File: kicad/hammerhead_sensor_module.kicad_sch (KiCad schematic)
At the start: 27 parts, among them J1 COMMS CONN, J10 12402012E212A, J9 B6B-XH-A, U16 TPD4E05U06DQAR, U4 TPD4E05U06DQAR

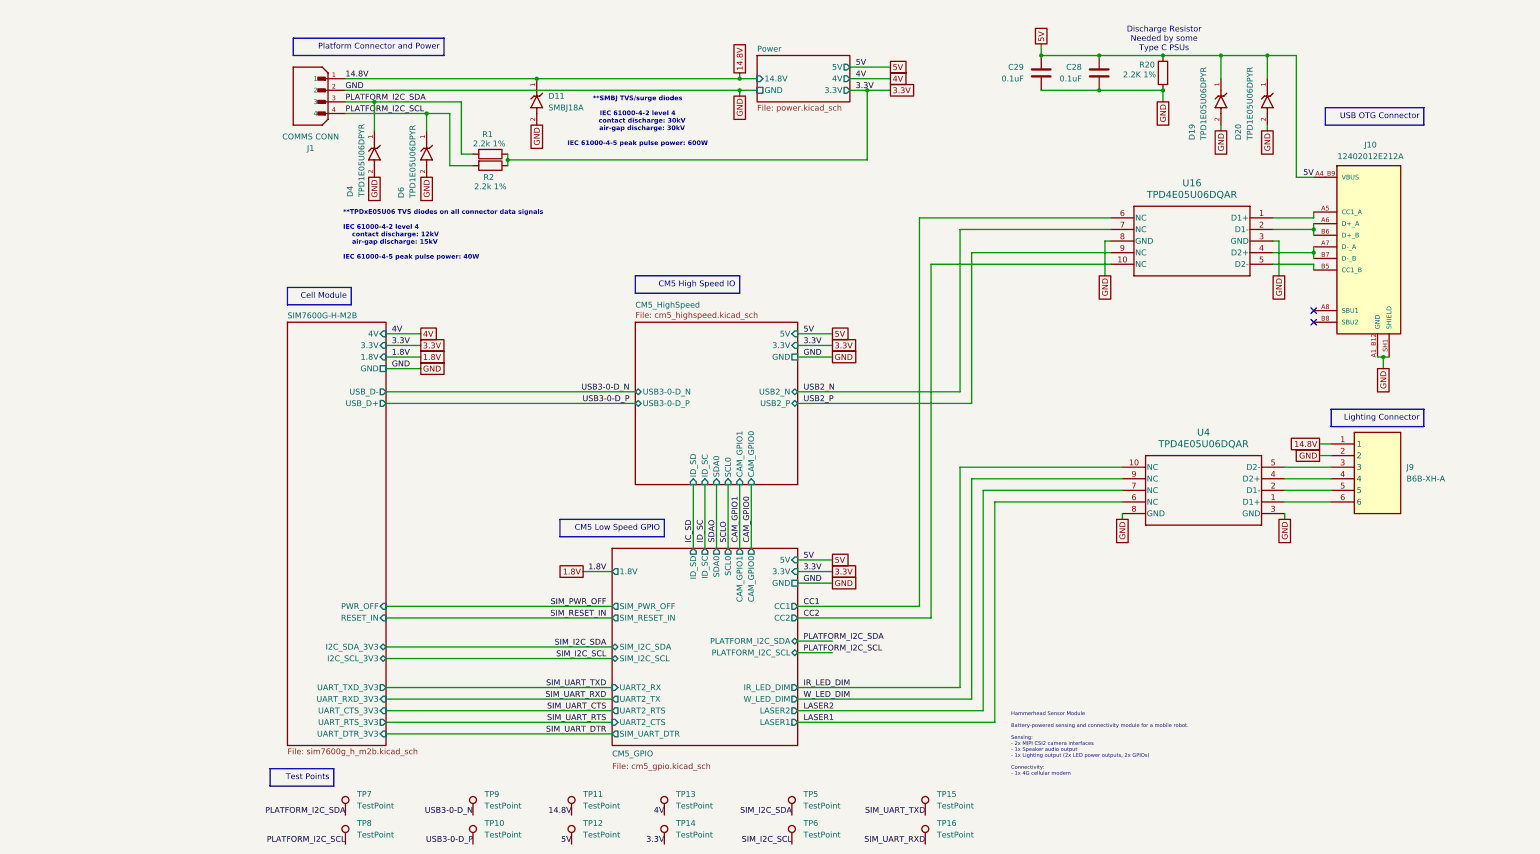
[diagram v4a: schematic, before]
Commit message: add can controller and transceiver, replace jst connectors with molex micro fit connectors
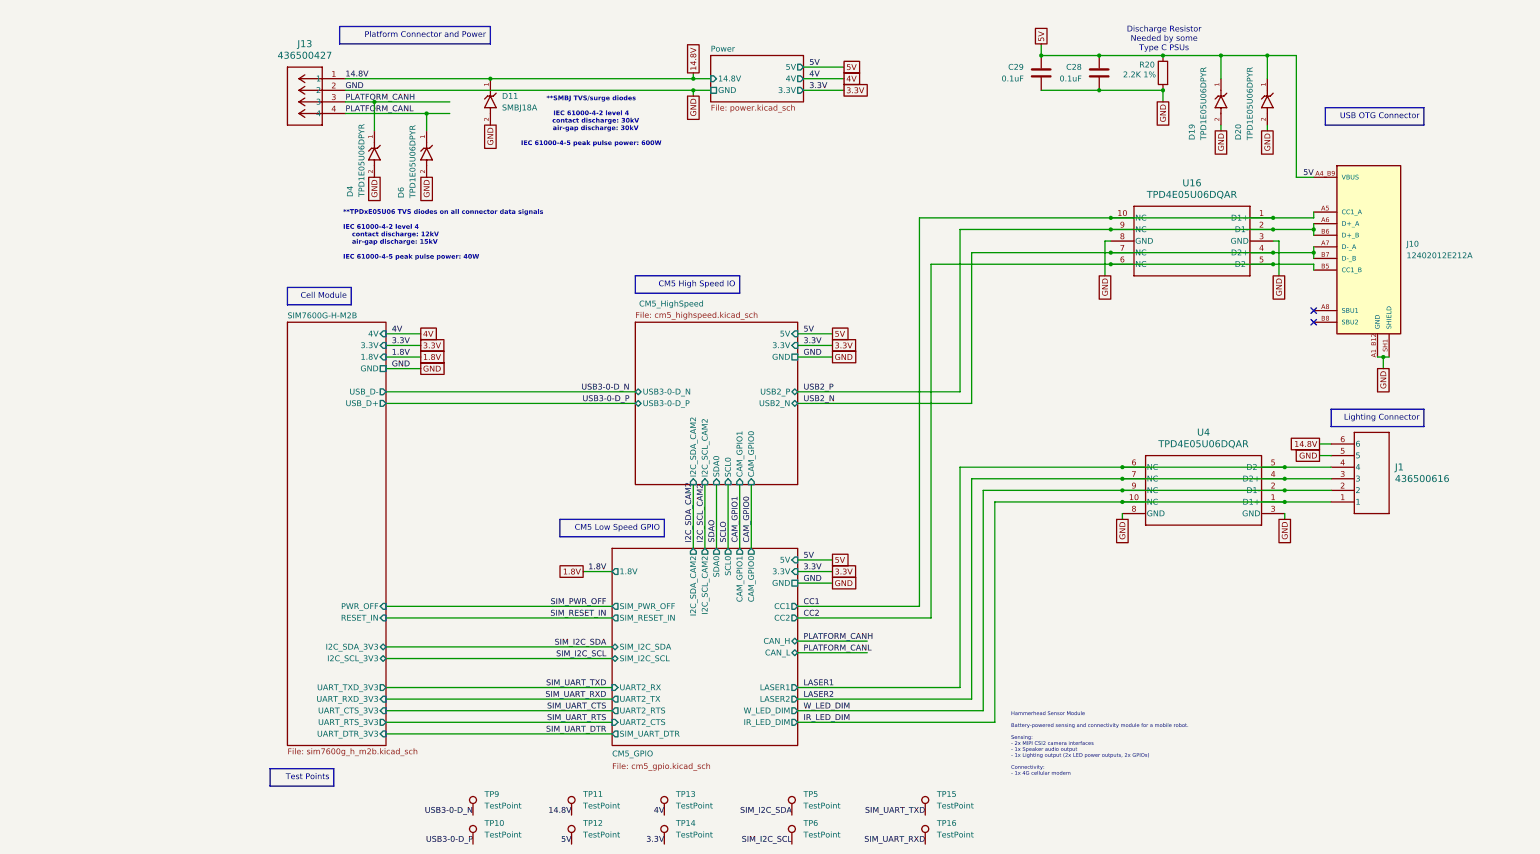
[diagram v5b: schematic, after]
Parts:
- removed J1: COMMS CONN, B4B-XH-A:JST_B4B-XH-A, symbol B4B-XH-A:B4B-XH-A
- removed J9: B6B-XH-A, B6B-XH-A:B6BXHA, symbol B6B-XH-A:B6B-XH-A
- removed R1, R2: 2.2k 1%, Resistor_SMD:R_0201_0603Metric, symbol Device:R
- removed TP7, TP8: TestPoint, TestPoint:TestPoint_Pad_1.0x1.0mm, symbol Connector:TestPoint
- added J1: 436500616, 436500616:CONN_SD-43650-006_06_MOL, symbol 436500616:436500616
- added J13: 436500427, 436500427:CONN_SD-43650-010_04_MOL, symbol 436500427:436500427
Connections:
- net 14.8V: now also J1.6, J13.1
- net CC1: now also J10.A5 (CC1_A), U16.1 (D1+), U16.10 (NC); no longer U16.6 (NC)
- net CC2: now also J10.B5 (CC1_B), U16.5 (D2-), U16.6 (NC); no longer U16.10 (NC)
- net GND: now also J1.5, J13.2
- net IR_LED_DIM: now also U4.1 (D1+), J1.1
- net LASER1: now also U4.5 (D2-), J1.4
- net LASER2: now also U4.4 (D2+), J1.3
- net USB2_N: now also J10.A7 (D-_A), J10.B7 (D-_B), U16.4 (D2+)
- net USB2_P: now also J10.A6 (D+_A), J10.B6 (D+_B), U16.2 (D1-)
- net W_LED_DIM: now also U4.2 (D1-), J1.2
- net PLATFORM_I2C_SCL renamed PLATFORM_CANL
- net PLATFORM_CANL: now also J13.4
- net PLATFORM_I2C_SDA renamed PLATFORM_CANH
- net PLATFORM_CANH: now also J13.3
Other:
- sheet CM5_GPIO ports: added CAN_H, CAN_L, I2C_SCL_CAM2, I2C_SDA_CAM2; removed ID_SC, ID_SD, PLATFORM_I2C_SCL, PLATFORM_I2C_SDA
- sheet CM5_HighSpeed ports: added I2C_SCL_CAM2, I2C_SDA_CAM2; removed ID_SC, ID_SD
- moved on the sheet: D11

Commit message: add can controller and transceiver, replace platform power connector with one with more appropriate current rating, add return vias
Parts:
- added GND1, GND2, GND3, GND4, TP21, TP22, TP23, TP24: TestPoint, TestPoint:TestPoint_Pad_1.0x1.0mm, symbol Connector:TestPoint
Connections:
- net GND: now also GND1.1, GND2.1, GND3.1, GND4.1
- net USB2_N: now also TP22.1
- net USB2_P: now also TP21.1
- new net TEST_GPIO_1: TP23.1
- new net TEST_GPIO_2: TP24.1
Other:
- sheet CM5_GPIO ports: added TEST_GPIO_1, TEST_GPIO_2; removed none
- moved on the sheet: TP10, TP11, TP12, TP13, TP14, TP15, TP16, TP5, TP6, TP9

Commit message: add board bringup redlines
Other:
- sheet CM5_GPIO ports: added GPIO_VREF; removed none
- sheet Power ports: added 3.3V_EN; removed none
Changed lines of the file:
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@@
 		)
 	)
+	(text_box "Issues\n- PWR_BUT should be floating, not tied to gnd\n- Tie GPIO_VREF to raspberry pi supplied 3.3v. Works fine without, but is outside design guidance. Look into this.\n- No protection between usb-c vbus and 5v net at output of buck converter. Bad things."
+		(exclude_from_sim no)
+		(at -41.91 12.7 0)
+		(size 50.8 17.78)
+		(margins 0.9525 0.9525 0.9525 0.9525)
+		(stroke
+			(width 0)
+			(type solid)
+		)
+		(fill
+			(type none)
+		)
+		(effects
+			(font
+				(size 1.27 1.27)
+			)
+			(justify left top)
+		)
+	)
+	(text_box "Add optional 0R resistor shorting shutdown pin on modem to 3.3v. optional dnp"
+		(exclude_from_sim no)
+		(at -41.91 31.75 0)
+		(size 50.8 6.35)
+		(margins 0.9525 0.9525 0.9525 0.9525)
+		(stroke
+			(width 0)
+			(type solid)
+		)
+		(fill
+			(type none)
+		)
+		(effects
+			(font
+				(size 1.27 1.27)
+			)
+			(justify left top)
+		)
+	)
 	(text_box "USB OTG Connector"
 		(exclude_from_sim no)
@@
 	)
 	(junction
-		(at 107.95 30.48)
-		(diameter 0)
-		(color 0 0 0 0)
-	)
-	(junction
 		(at 184.15 22.86)
 		(diameter 0)
@@
 	)
 	(junction
-		(at 237.49 115.57)
+		(at 102.87 30.48)
 		(diameter 0)
 		(color 0 0 0 0)
 	)
 	(junction
-		(at 243.84 66.04)
+		(at 237.49 115.57)
 		(diameter 0)
 		(color 0 0 0 0)
 	)
 	(junction
-		(at 107.95 27.94)
+		(at 243.84 66.04)
 		(diameter 0)
 		(color 0 0 0 0)
@@
 	)
 	(junction
+		(at 102.87 27.94)
+		(diameter 0)
+		(color 0 0 0 0)
+	)
+	(junction
 		(at 234.95 66.04)
 		(diameter 0)
@@
 	(wire
 		(pts
-			(xy 90.17 135.89) (xy 83.82 135.89)
+			(xy 90.17 135.89) (xy 76.2 135.89)
 		)
 		(stroke
@@
 	(wire
 		(pts
-			(xy 132.08 27.94) (xy 140.97 27.94)
+			(xy 140.97 27.94) (xy 149.86 27.94)
+		)
+		(stroke
+			(width 0)
+			(type default)
+		)
+	)
+	(wire
+		(pts
+			(xy 74.93 138.43) (xy 90.17 138.43)
 		)
 		(stroke
@@
 	(wire
 		(pts
-			(xy 132.08 30.48) (xy 140.97 30.48)
+			(xy 140.97 30.48) (xy 149.86 30.48)
 		)
 		(stroke
@@
 	(wire
 		(pts
+			(xy 102.87 27.94) (xy 120.65 27.94)
+		)
+		(stroke
+			(width 0)
+			(type default)
+		)
+	)
+	(wire
+		(pts
 			(xy 243.84 64.77) (xy 243.84 66.04)
 		)
@@
 	(wire
 		(pts
-			(xy 63.5 27.94) (xy 107.95 27.94)
+			(xy 63.5 27.94) (xy 102.87 27.94)
 		)
 		(stroke
@@
 	(wire
 		(pts
-			(xy 107.95 27.94) (xy 111.76 27.94)
-		)
-		(stroke
-			(width 0)
-			(type default)
-		)
-	)
-	(wire
-		(pts
 			(xy 233.68 22.86) (xy 233.68 27.94)
 		)
@@
 	(wire
 		(pts
-			(xy 107.95 26.67) (xy 107.95 27.94)
+			(xy 102.87 26.67) (xy 102.87 27.94)
 		)
 		(stroke
@@
 	(wire
 		(pts
-			(xy 132.08 25.4) (xy 140.97 25.4)
+			(xy 140.97 25.4) (xy 149.86 25.4)
 		)
 		(stroke
@@
 	(wire
 		(pts
-			(xy 107.95 30.48) (xy 111.76 30.48)
-		)
-		(stroke
-			(width 0)
-			(type default)
-		)
-	)
-	(wire
-		(pts
 			(xy 234.95 60.96) (xy 243.84 60.96)
 		)
@@
 	(wire
 		(pts
+			(xy 107.95 25.4) (xy 120.65 25.4)
+		)
+		(stroke
+			(width 0)
+			(type default)
+		)
+	)
+	(wire
+		(pts
 			(xy 168.91 99.06) (xy 130.81 99.06)
 		)
@@
 	(wire
 		(pts
-			(xy 31.75 30.48) (xy 107.95 30.48)
+			(xy 31.75 30.48) (xy 102.87 30.48)
 		)
 		(stroke
@@
 	(wire
 		(pts
+			(xy 102.87 30.48) (xy 120.65 30.48)
+		)
+		(stroke
+			(width 0)
+			(type default)
+		)
+	)
+	(wire
+		(pts
 			(xy 160.02 68.58) (xy 199.39 68.58)
 		)
@@
 	(wire
 		(pts
-			(xy 107.95 31.75) (xy 107.95 30.48)
+			(xy 102.87 31.75) (xy 102.87 30.48)
 		)
 		(stroke
@@
 	)
 	(label "3.3V"
-		(at 133.35 30.48 0)
+		(at 142.24 30.48 0)
 		(effects
 			(font
@@
 	)
 	(label "5V"
-		(at 133.35 25.4 0)
+		(at 142.24 25.4 0)
 		(effects
 			(font
@@
 		)
 	)
+	(label "GPIO_VREF"
+		(at 88.9 138.43 180)
+		(effects
+			(font
+				(size 1.27 1.27)
+			)
+			(justify right bottom)
+		)
+	)
 	(label "SIM_RESET_IN"
 		(at 88.9 146.05 180)
@@
 	)
 	(label "4V"
-		(at 133.35 27.94 0)
+		(at 142.24 27.94 0)
 		(effects
 			(font
@@
 		)
 	)
+	(label "GPIO_VREF"
+		(at 119.38 25.4 180)
+		(effects
+			(font
+				(size 1.27 1.27)
+			)
+			(justify right bottom)
+		)
+	)
 	(global_label "GND"
 		(shape passive)
@@
 	(global_label "3.3V"
 		(shape passive)
-		(at 140.97 30.48 0)
+		(at 149.86 30.48 0)
 		(fields_autoplaced yes)
 		(effects
@@
 		)
 		(property "Intersheetrefs" "${INTERSHEET_REFS}"
-			(at 146.9563 30.48 0)
+			(at 155.8463 30.48 0)
 			(effects
 				(font
@@
 	(global_label "GND"
 		(shape passive)
-		(at 107.95 31.75 270)
+		(at 102.87 31.75 270)
 		(fields_autoplaced yes)
 		(effects
@@
 		)
 		(property "Intersheetrefs" "${INTERSHEET_REFS}"
-			(at 107.95 37.4944 90)
+			(at 102.87 37.4944 90)
 			(effects
 				(font
@@
 	(global_label "1.8V"
 		(shape passive)
-		(at 83.82 135.89 180)
+		(at 76.2 135.89 180)
 		(fields_autoplaced yes)
 		(effects
@@
 		)
 		(property "Intersheetrefs" "${INTERSHEET_REFS}"
-			(at 77.8337 135.89 0)
+			(at 70.2137 135.89 0)
 			(effects
 				(font
@@
 	(global_label "4V"
 		(shape passive)
-		(at 140.97 27.94 0)
+		(at 149.86 27.94 0)
 		(fields_autoplaced yes)
 		(effects
@@
 		)
 		(property "Intersheetrefs" "${INTERSHEET_REFS}"
-			(at 145.142 27.94 0)
+			(at 154.032 27.94 0)
 			(effects
 				(font
@@
 	(global_label "5V"
 		(shape passive)
-		(at 140.97 25.4 0)
+		(at 149.86 25.4 0)
 		(fields_autoplaced yes)
 		(effects
@@
 		)
 		(property "Intersheetrefs" "${INTERSHEET_REFS}"
-			(at 145.142 25.4 0)
+			(at 154.032 25.4 0)
 			(effects
 				(font
@@
 	(global_label "14.8V"
 		(shape passive)
-		(at 107.95 26.67 90)
+		(at 102.87 26.67 90)
 		(fields_autoplaced yes)
 		(effects
@@
 		)
 		(property "Intersheetrefs" "${INTERSHEET_REFS}"
-			(at 107.95 19.4742 90)
+			(at 102.87 19.4742 90)
 			(effects
 				(font
@@
 			)
 		)
+		(pin "GPIO_VREF" output
+			(at 90.17 138.43 180)
+			(effects
+				(font
+					(size 1.27 1.27)
+				)
+				(justify left)
+			)
+		)
 		(instances
 			(project "hammerhead_sensor_module"
@@
 	)
 	(sheet
-		(at 111.76 22.86)
+		(at 120.65 22.86)
 		(size 20.32 10.16)
 		(exclude_from_sim no)
@@
 		)
 		(property "Sheetname" "Power"
-			(at 111.76 22.1484 0)
+			(at 120.65 22.1484 0)
 			(effects
 				(font
@@
 		)
 		(property "Sheetfile" "power.kicad_sch"
-			(at 111.76 33.6046 0)
+			(at 120.65 33.6046 0)
 			(effects
 				(font
@@
 		)
 		(pin "5V" output
-			(at 132.08 25.4 0)
+			(at 140.97 25.4 0)
 			(effects
 				(font
@@
 		)
 		(pin "GND" passive
-			(at 111.76 30.48 180)
+			(at 120.65 30.48 180)
 			(effects
 				(font
@@
 		)
 		(pin "4V" output
-			(at 132.08 27.94 0)
+			(at 140.97 27.94 0)
 			(effects
 				(font
@@
 		)
 		(pin "14.8V" input
-			(at 111.76 27.94 180)
+			(at 120.65 27.94 180)
 			(effects
 				(font
@@
 		)
 		(pin "3.3V" output
-			(at 132.08 30.48 0)
+			(at 140.97 30.48 0)
 			(effects
 				(font
@@
 			)
 		)
+		(pin "3.3V_EN" input
+			(at 120.65 25.4 180)
+			(effects
+				(font
+					(size 1.27 1.27)
+				)
+				(justify left)
+			)
+		)
